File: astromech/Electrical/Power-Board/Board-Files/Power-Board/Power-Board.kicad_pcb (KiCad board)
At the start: 2 copper layers, 119.4 x 96.5 mm, 4 parts

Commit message: loaded components into board
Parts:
- added 12V1: Generic_Power_Out, astromech-footprints:Phoenix-1935161, F.Cu at (263.1, 99.7)
- added 12V2: Generic_Power_Out, astromech-footprints:Phoenix-1935161, F.Cu at (228.2, 116.8)
- added 12V3: Generic_Power_Out, astromech-footprints:Phoenix-1935161, F.Cu at (251.7, 80.9)
- added 12V4: Generic_Power_Out, astromech-footprints:Phoenix-1935161, F.Cu at (239.8, 111.0)
- added 3.3V1: Generic_Power_Out, astromech-footprints:Phoenix-1935161, F.Cu at (251.5, 101.6)
- added 3.3V2: Generic_Power_Out, astromech-footprints:Phoenix-1935161, F.Cu at (251.5, 111.0)
- added 3.3V3: Generic_Power_Out, astromech-footprints:Phoenix-1935161, F.Cu at (280.5, 92.1)
- added 3.3V4: Generic_Power_Out, astromech-footprints:Phoenix-1935161, F.Cu at (297.6, 63.8)
- added 5V1: Generic_Power_Out, astromech-footprints:Phoenix-1935161, F.Cu at (280.5, 82.6)
- added 5V2: Generic_Power_Out, astromech-footprints:Phoenix-1935161, F.Cu at (286.0, 63.8)
- added 5V3: Generic_Power_Out, astromech-footprints:Phoenix-1935161, F.Cu at (263.1, 109.2)
- added 5V4: Generic_Power_Out, astromech-footprints:Phoenix-1935161, F.Cu at (289.8, 54.4)
- added C1: 0.1uF, Capacitor_SMD:C_1206_3216Metric_Pad1.33x1.80mm_HandSolder, F.Cu at (237.3, 117.6)
- added C2: 1u, Capacitor_SMD:C_1206_3216Metric_Pad1.33x1.80mm_HandSolder, F.Cu at (272.2, 102.2)
- added C3: C_T, Capacitor_SMD:C_1206_3216Metric_Pad1.33x1.80mm_HandSolder, F.Cu at (249.4, 117.6)
- added C4: 0.1uF, Capacitor_SMD:C_1206_3216Metric_Pad1.33x1.80mm_HandSolder, F.Cu at (243.3, 117.6)
- added C5: 0.1uF, Capacitor_SMD:C_1206_3216Metric_Pad1.33x1.80mm_HandSolder, F.Cu at (205.1, 118.1)
- added C6: 1u, Capacitor_SMD:C_1206_3216Metric_Pad1.33x1.80mm_HandSolder, F.Cu at (255.4, 117.6)
- added C7: C_T, Capacitor_SMD:C_1206_3216Metric_Pad1.33x1.80mm_HandSolder, F.Cu at (211.1, 118.1)
- added C8: 0.1uF, Capacitor_SMD:C_1206_3216Metric_Pad1.33x1.80mm_HandSolder, F.Cu at (217.1, 118.1)
- added F1: F_MAIN, Fuse:Fuseholder_Blade_Mini_Keystone_3568, F.Cu at (258.9, 52.3)
- added HV_OUT1: HV_OUT, astromech-footprints:Phoenix-1935161, F.Cu at (313.0, 54.4)
- added HV_OUT2: HV_OUT, astromech-footprints:Phoenix-1935161, F.Cu at (234.1, 92.2)
- added HV_OUT3: HV_OUT, astromech-footprints:Phoenix-1935161, F.Cu at (257.3, 90.3)
- added HV_OUT4: HV_OUT, astromech-footprints:Phoenix-1935161, F.Cu at (228.2, 107.4)
- added J1: BAT_IN_SCREW, astromech-footprints:Molex-393900102, F.Cu at (81.3, 91.4)
- added J10: HEAD_MOT, astromech-footprints:Phoenix-1935161, F.Cu at (274.9, 73.2)
- added J2: BAT_IN_HOLE, astromech-footprints:10AWG-Power-In, F.Cu at (96.5, 91.4)
- added J5: E_STOP, astromech-footprints:Phoenix-1935161, F.Cu at (268.9, 88.5)
- added J6: CTRL_BRD, astromech-footprints:Phoenix-1935161, F.Cu at (301.4, 54.4)
- added J7: JETSON, astromech-footprints:Phoenix-1935161, F.Cu at (286.6, 73.2)
- added J8: L_DRIVE, astromech-footprints:Phoenix-1935161, F.Cu at (274.4, 63.8)
- added J9: R_DRIVE, astromech-footprints:Phoenix-1935161, F.Cu at (239.8, 101.6)
- added LV_IN1: LV_IN, astromech-footprints:Phoenix-1935161, F.Cu at (263.3, 79.0)
- added LV_IN2: LV_IN, astromech-footprints:Phoenix-1935161, F.Cu at (278.2, 54.4)
- added LV_IN3: LV_IN, astromech-footprints:Phoenix-1935161, F.Cu at (245.7, 92.2)
- added LV_IN4: LV_IN, astromech-footprints:Phoenix-1935161, F.Cu at (298.2, 73.2)
- added Q1: Q_NMOS_DSG, astromech-footprints:NTMTS0D6N04CLTXG, F.Cu at (308.9, 64.5)
- added Q2: Q_NMOS_DSG, astromech-footprints:NTMTS0D6N04CLTXG, F.Cu at (291.2, 83.4)
- added R1: 220k, Resistor_SMD:R_1206_3216Metric_Pad1.30x1.75mm_HandSolder, F.Cu at (327.7, 51.5)
- added R10: 100k, Resistor_SMD:R_1206_3216Metric_Pad1.30x1.75mm_HandSolder, F.Cu at (316.4, 64.2)
- added R11: R_FLT, Resistor_SMD:R_1206_3216Metric_Pad1.30x1.75mm_HandSolder, F.Cu at (316.4, 60.9)
- added R12: R_G, Resistor_SMD:R_1206_3216Metric_Pad1.30x1.75mm_HandSolder, F.Cu at (278.1, 101.9)
- added R2: 100k, Resistor_SMD:R_1206_3216Metric_Pad1.30x1.75mm_HandSolder, F.Cu at (322.4, 58.7)
- added R3: 100k, Resistor_SMD:R_1206_3216Metric_Pad1.30x1.75mm_HandSolder, F.Cu at (289.6, 90.2)
- added R4: 100k, Resistor_SMD:R_1206_3216Metric_Pad1.30x1.75mm_HandSolder, F.Cu at (307.2, 71.3)
- added R5: R_FLT, Resistor_SMD:R_1206_3216Metric_Pad1.30x1.75mm_HandSolder, F.Cu at (261.3, 119.0)
- added R6: R_G, Resistor_SMD:R_1206_3216Metric_Pad1.30x1.75mm_HandSolder, F.Cu at (298.8, 79.7)
- added R7: 220k, Resistor_SMD:R_1206_3216Metric_Pad1.30x1.75mm_HandSolder, F.Cu at (277.8, 98.6)
- added R8: 100k, Resistor_SMD:R_1206_3216Metric_Pad1.30x1.75mm_HandSolder, F.Cu at (272.1, 105.5)
- added R9: 100k, Resistor_SMD:R_1206_3216Metric_Pad1.30x1.75mm_HandSolder, F.Cu at (261.3, 115.7)
- added TP1: TestPoint, TestPoint:TestPoint_Pad_D2.0mm, F.Cu at (271.4, 80.1)
- added TP2: TestPoint, TestPoint:TestPoint_Pad_D2.0mm, F.Cu at (230.6, 99.1)
- added U1: LTC7003, astromech-footprints:LTC7003, F.Cu at (272.0, 96.9)
- added U2: Logic_Level_Converter, astromech-footprints:Sparkfun-Level-shifter, F.Cu at (262.0, 66.5)
- added U3: D36V50Fx, astromech-footprints:D36V50Fx, F.Cu at (215.3, 63.1)
- added U4: LTC7003, astromech-footprints:LTC7003, F.Cu at (321.9, 53.4)
- added U5: D36V50Fx, astromech-footprints:D36V50Fx, F.Cu at (215.3, 89.6)
- added U6: D36V50Fx, astromech-footprints:D36V50Fx, F.Cu at (241.8, 63.1)

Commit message: grouped related components and did minor layout
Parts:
- U3: value D36V50Fx -> 12V_REG
- U5: value D36V50Fx -> 5V_REG
- U6: value D36V50Fx -> 3.3V_REG
- moved U5 194.0 mm to (405.1, 129.5)
- moved R2 191.1 mm to (138.4, 110.5)
- moved R1 189.8 mm to (147.3, 110.5)
- moved HV_OUT4 172.9 mm to (391.2, 49.5)
- moved R4 169.2 mm to (138.4, 83.0)
- moved F1 160.8 mm to (99.9, 76.1), turned to 90 degrees
- moved R3 151.2 mm to (138.4, 94.5), turned to 180 degrees
- moved 5V3 149.7 mm to (412.8, 111.8)
- moved 5V4 147.3 mm to (425.4, 111.8)
- moved Q1 143.2 mm to (170.2, 100.3)
- moved R6 138.4 mm to (162.6, 104.1)
- moved C2 133.8 mm to (138.4, 99.5), turned to 180 degrees
- moved 5V2 123.7 mm to (400.1, 111.8)
- moved U1 120.9 mm to (151.1, 95.2), turned to -90 degrees
- moved TP1 117.2 mm to (156.2, 101.6)
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
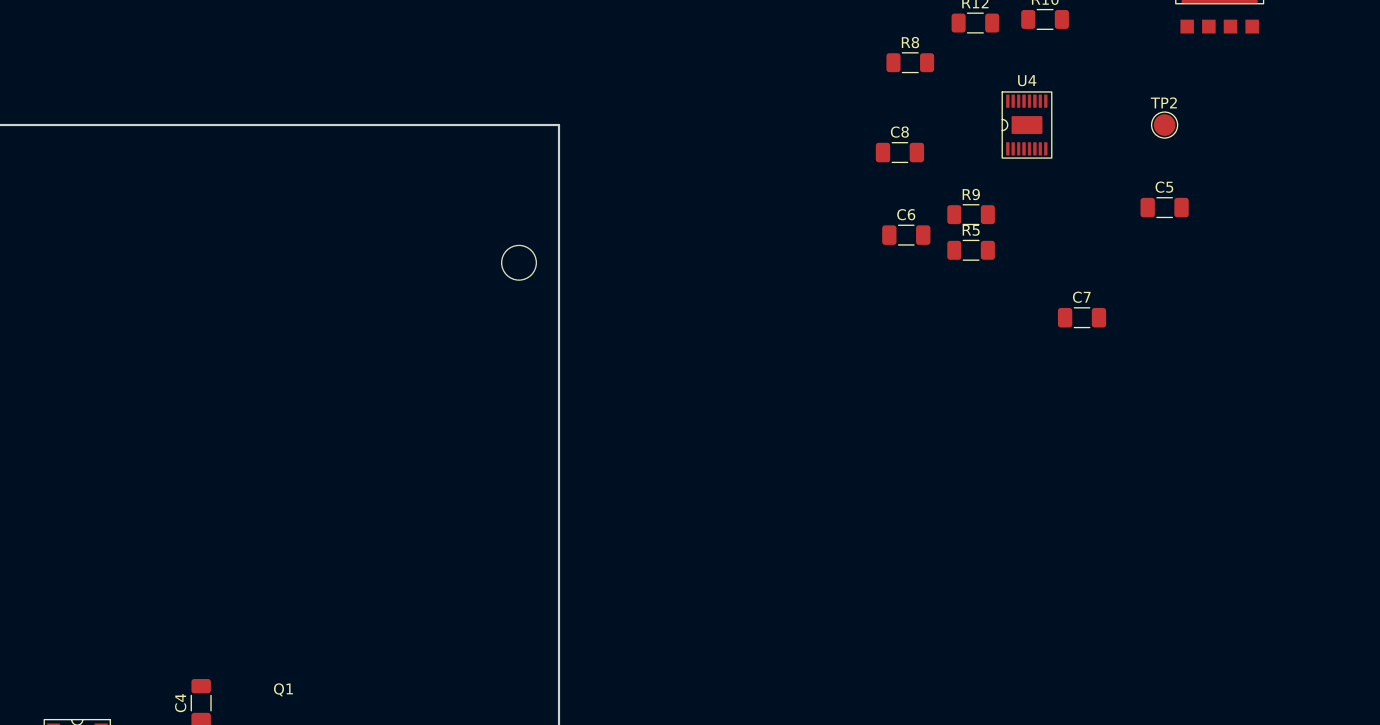
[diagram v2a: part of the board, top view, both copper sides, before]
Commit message: Assigned shottky diode footprints
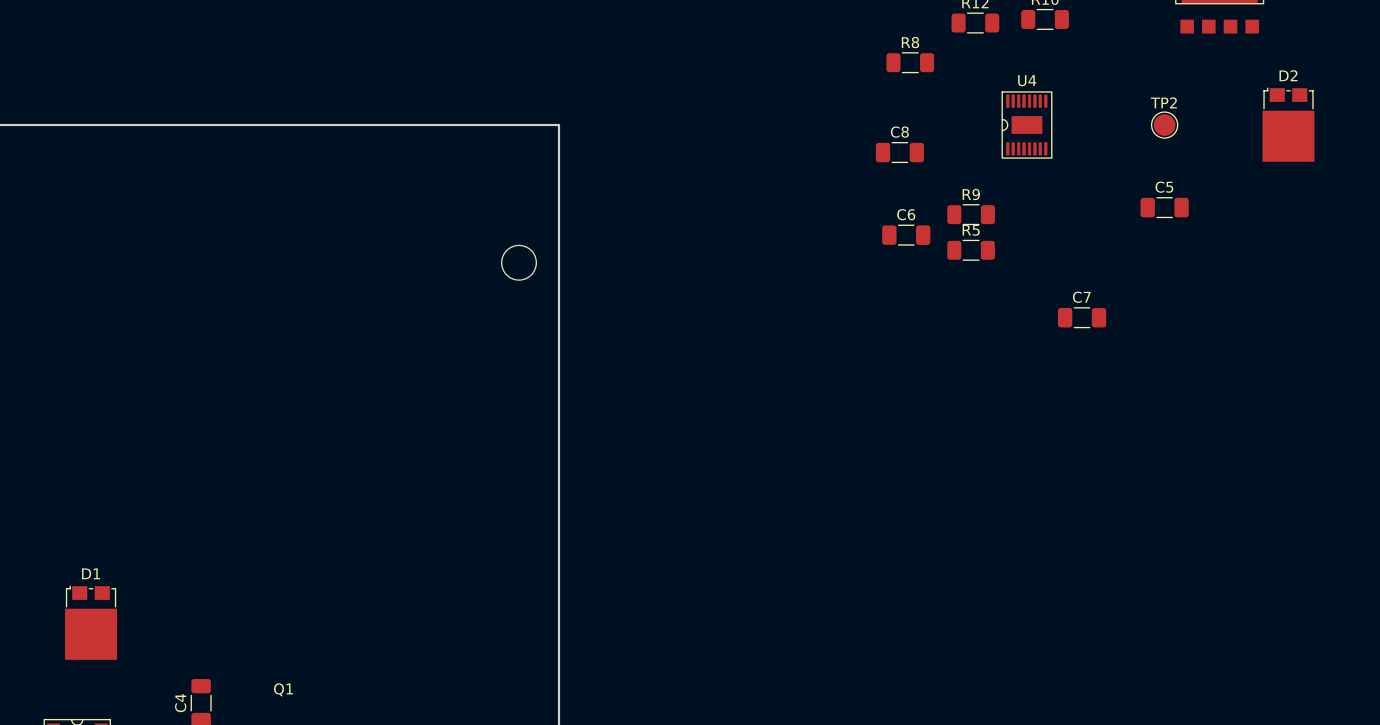
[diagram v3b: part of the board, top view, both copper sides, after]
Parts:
- added D1: D_Schottky_AAK, Package_TO_SOT_SMD:TO-277A, F.Cu at (152.4, 84.0)
- added D2: D_Schottky_AAK, Package_TO_SOT_SMD:TO-277A, F.Cu at (262.9, 38.1)
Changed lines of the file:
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@@
   (net 54 "unconnected-(U6-Pad5)")
   (net 55 "unconnected-(U6-Pad6)")
+  (net 56 "unconnected-(D2-Pad1)")
   (footprint "Resistor_SMD:R_1206_3216Metric_Pad1.30x1.75mm_HandSolder" (layer "F.Cu")
     (at 233.6025 49.66)
@@
     (pad "2" thru_hole roundrect (at 2.54 0) (size 2 4.5) (drill 1.3) (layers *.Cu *.Mask) (roundrect_rratio 0.5)
       (net 3 "5V_REG") (pinfunction "+") (pintype "power_in"))
+  )
+  (footprint "Package_TO_SOT_SMD:TO-277A" (layer "F.Cu")
+    (at 152.4 84.05)
+    (descr "Thermal enhanced ultra thin SMD package; 3 leads; body: 4.3x6.1x0.43mm, https://www.vishay.com/docs/95570/to-277asmpc.pdf")
+    (tags "TO-277A SMPC")
+    (property "Sheetfile" "Power-Board.kicad_sch")
+    (property "Sheetname" "")
+    (attr smd)
+    (fp_text reference "D1" (at 0 -4.5 -180) (layer "F.SilkS")
+      (effects (font (size 1 1) (thickness 0.15)))
+    )
+    (fp_text value "D_Schottky_AAK" (at 0 4.5 -180) (layer "F.Fab")
+      (effects (font (size 1 1) (thickness 0.15)))
+    )
+    (fp_text user "${REFERENCE}" (at 0 0) (layer "F.Fab")
+      (effects (font (size 1 1) (thickness 0.15)))
+    )
+    (fp_line (start 2.26 -1.5) (end 2.26 -3.16) (layer "F.SilkS") (width 0.12))
+    (fp_line (start -1.92 -3.4) (end -1.92 -3.16) (layer "F.SilkS") (width 0.12))
+    (fp_line (start 2.26 -3.16) (end 1.92 -3.16) (layer "F.SilkS") (width 0.12))
+    (fp_line (start -0.16 -3.16) (end 0.16 -3.16) (layer "F.SilkS") (width 0.12))
+    (fp_line (start -2.26 -3.16) (end -2.26 -1.5) (layer "F.SilkS") (width 0.12))
+    (fp_line (start -1.92 -3.16) (end -2.26 -3.16) (layer "F.SilkS") (width 0.12))
+    (fp_line (start 2.65 3.65) (end -2.65 3.65) (layer "F.CrtYd") (width 0.05))
+    (fp_line (start -2.65 -3.65) (end 2.65 -3.65) (layer "F.CrtYd") (width 0.05))
+    (fp_line (start -2.65 -3.65) (end -2.65 3.65) (layer "F.CrtYd") (width 0.05))
+    (fp_line (start 2.65 3.65) (end 2.65 -3.65) (layer "F.CrtYd") (width 0.05))
+    (fp_line (start 2.15 3.05) (end 2.15 -3.05) (layer "F.Fab") (width 0.1))
+    (fp_line (start 2.15 -3.05) (end -1.15 -3.05) (layer "F.Fab") (width 0.1))
+    (fp_line (start -2.15 3.05) (end 2.15 3.05) (layer "F.Fab") (width 0.1))
+    (fp_line (start -1.15 -3.05) (end -2.15 -2.05) (layer "F.Fab") (width 0.1))
+    (fp_line (start -2.15 -2.05) (end -2.15 3.05) (layer "F.Fab") (width 0.1))
+    (pad "" smd rect (at -1.7 -0.65 180) (size 1.25 1.2) (layers "F.Paste"))
+    (pad "" smd rect (at 1.7 2.7) (size 1.25 1.2) (layers "F.Paste"))
+    (pad "" smd rect (at 1.7 1.04) (size 1.25 1.2) (layers "F.Paste"))
+    (pad "" smd rect (at 0 1.04) (size 1.25 1.2) (layers "F.Paste"))
+    (pad "" smd rect (at -1.7 2.7) (size 1.25 1.2) (layers "F.Paste"))
+    (pad "" smd rect (at -1.7 1.04) (size 1.25 1.2) (layers "F.Paste"))
+    (pad "" smd rect (at 0 -0.65) (size 1.25 1.2) (layers "F.Paste"))
+    (pad "" smd rect (at 0 2.7) (size 1.25 1.2) (layers "F.Paste"))
+    (pad "" smd rect (at 1.7 -0.65) (size 1.25 1.2) (layers "F.Paste"))
+    (pad "1" smd rect (at -1.04 -2.765) (size 1.4 1.27) (layers "F.Cu" "F.Paste" "F.Mask")
+      (net 1 "GND") (pinfunction "A") (pintype "passive"))
+    (pad "2" smd rect (at 1.04 -2.765) (size 1.4 1.27) (layers "F.Cu" "F.Paste" "F.Mask")
+      (net 1 "GND") (pinfunction "A") (pintype "passive"))
+    (pad "3" smd rect (at 0 1.04) (size 4.8 4.72) (layers "F.Cu" "F.Mask")
+      (net 9 "+BATT") (pinfunction "K") (pintype "passive"))
+    (model "${KICAD6_3DMODEL_DIR}/Package_TO_SOT_SMD.3dshapes/TO-277A.wrl"
+      (offset (xyz 0 0 0))
+      (scale (xyz 1 1 1))
+      (rotate (xyz 0 0 0))
+    )
   )
   (footprint "astromech-footprints:Phoenix-1935161" (layer "F.Cu")
@@
       (offset (xyz 0 0 0))
       (scale (xyz 1 1 1))
+      (rotate (xyz 0 0 0))
+    )
+  )
+  (footprint "Package_TO_SOT_SMD:TO-277A" (layer "F.Cu")
+    (at 262.89 38.1)
+    (descr "Thermal enhanced ultra thin SMD package; 3 leads; body: 4.3x6.1x0.43mm, https://www.vishay.com/docs/95570/to-277asmpc.pdf")
+    (tags "TO-277A SMPC")
+    (property "Sheetfile" "Power-Board.kicad_sch")
+    (property "Sheetname" "")
+    (attr smd)
+    (fp_text reference "D2" (at 0 -4.5 -180) (layer "F.SilkS")
+      (effects (font (size 1 1) (thickness 0.15)))
+    )
+    (fp_text value "D_Schottky_AAK" (at 0 4.5 -180) (layer "F.Fab")
+      (effects (font (size 1 1) (thickness 0.15)))
+    )
+    (fp_text user "${REFERENCE}" (at 0 0) (layer "F.Fab")
+      (effects (font (size 1 1) (thickness 0.15)))
+    )
+    (fp_line (start -1.92 -3.4) (end -1.92 -3.16) (layer "F.SilkS") (width 0.12))
+    (fp_line (start 2.26 -1.5) (end 2.26 -3.16) (layer "F.SilkS") (width 0.12))
+    (fp_line (start 2.26 -3.16) (end 1.92 -3.16) (layer "F.SilkS") (width 0.12))
+    (fp_line (start -2.26 -3.16) (end -2.26 -1.5) (layer "F.SilkS") (width 0.12))
+    (fp_line (start -1.92 -3.16) (end -2.26 -3.16) (layer "F.SilkS") (width 0.12))
+    (fp_line (start -0.16 -3.16) (end 0.16 -3.16) (layer "F.SilkS") (width 0.12))
+    (fp_line (start 2.65 3.65) (end -2.65 3.65) (layer "F.CrtYd") (width 0.05))
+    (fp_line (start -2.65 -3.65) (end -2.65 3.65) (layer "F.CrtYd") (width 0.05))
+    (fp_line (start -2.65 -3.65) (end 2.65 -3.65) (layer "F.CrtYd") (width 0.05))
+    (fp_line (start 2.65 3.65) (end 2.65 -3.65) (layer "F.CrtYd") (width 0.05))
+    (fp_line (start -1.15 -3.05) (end -2.15 -2.05) (layer "F.Fab") (width 0.1))
+    (fp_line (start -2.15 -2.05) (end -2.15 3.05) (layer "F.Fab") (width 0.1))
+    (fp_line (start -2.15 3.05) (end 2.15 3.05) (layer "F.Fab") (width 0.1))
+    (fp_line (start 2.15 -3.05) (end -1.15 -3.05) (layer "F.Fab") (width 0.1))
+    (fp_line (start 2.15 3.05) (end 2.15 -3.05) (layer "F.Fab") (width 0.1))
+    (pad "" smd rect (at 1.7 1.04) (size 1.25 1.2) (layers "F.Paste"))
+    (pad "" smd rect (at -1.7 2.7) (size 1.25 1.2) (layers "F.Paste"))
+    (pad "" smd rect (at -1.7 -0.65 180) (size 1.25 1.2) (layers "F.Paste"))
+    (pad "" smd rect (at -1.7 1.04) (size 1.25 1.2) (layers "F.Paste"))
+    (pad "" smd rect (at 1.7 -0.65) (size 1.25 1.2) (layers "F.Paste"))
+    (pad "" smd rect (at 0 2.7) (size 1.25 1.2) (layers "F.Paste"))
+    (pad "" smd rect (at 0 -0.65) (size 1.25 1.2) (layers "F.Paste"))
+    (pad "" smd rect (at 1.7 2.7) (size 1.25 1.2) (layers "F.Paste"))
+    (pad "" smd rect (at 0 1.04) (size 1.25 1.2) (layers "F.Paste"))
+    (pad "1" smd rect (at -1.04 -2.765) (size 1.4 1.27) (layers "F.Cu" "F.Paste" "F.Mask")
+      (net 56 "unconnected-(D2-Pad1)") (pinfunction "A") (pintype "passive"))
+    (pad "2" smd rect (at 1.04 -2.765) (size 1.4 1.27) (layers "F.Cu" "F.Paste" "F.Mask")
+      (net 1 "GND") (pinfunction "A") (pintype "passive"))
+    (pad "3" smd rect (at 0 1.04) (size 4.8 4.72) (layers "F.Cu" "F.Mask")
+      (net 13 "MOT_VOLTAGE") (pinfunction "K") (pintype "passive"))
+    (model "${KICAD6_3DMODEL_DIR}/Package_TO_SOT_SMD.3dshapes/TO-277A.wrl"
+      (offset (xyz 0 0 0))
+      (scale (xyz 1 1 1))

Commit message: Modified level converter connections
Made to fit NEO encoder connection order
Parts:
- added C10: C_G, Capacitor_SMD:C_1206_3216Metric_Pad1.33x1.80mm_HandSolder, F.Cu at (151.1, 124.8)
- added C9: C_G, Capacitor_SMD:C_1206_3216Metric_Pad1.33x1.80mm_HandSolder, F.Cu at (381.0, 234.3)
- added R13: R_CGDAMP, Resistor_SMD:R_1206_3216Metric_Pad1.30x1.75mm_HandSolder, F.Cu at (151.1, 140.3)
- added R14: R_CGDAMP, Resistor_SMD:R_1206_3216Metric_Pad1.30x1.75mm_HandSolder, F.Cu at (151.1, 117.9)
- moved R5 169.4 mm to (75.6, 110.7)
- moved R7 137.4 mm to (123.2, 107.1), turned to 90 degrees
- moved R8 132.1 mm to (123.2, 112.8), turned to 90 degrees
- moved Q2 131.7 mm to (137.2, 80.6), turned to 90 degrees
- moved TP2 127.9 mm to (156.8, 124.2)
- moved C5 127.1 mm to (138.4, 103.9), turned to -90 degrees
- moved D2 122.8 mm to (162.6, 109.0), turned to 180 degrees
- moved J5 121.1 mm to (125.7, 55.2), turned to 180 degrees
- moved R10 120.9 mm to (143.5, 100.7), turned to -90 degrees
- moved C7 118.3 mm to (138.4, 109.6), turned to -90 degrees
- moved J10 118.2 mm to (114.4, 55.2), turned to 180 degrees
- moved R12 117.9 mm to (156.8, 117.9), turned to -90 degrees
- moved R9 117.2 mm to (133.3, 107.1), turned to -90 degrees
- moved J9 117.0 mm to (103.0, 55.2), turned to 180 degrees
- moved J8 115.8 mm to (91.5, 55.2), turned to 180 degrees
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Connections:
- D2 pad 1: unconnected-(D2-Pad1) -> GND
- R12 pad 1: Net-(R12-Pad1) -> Net-(U4-Pad12)
- R6 pad 1: Net-(R6-Pad1) -> Net-(U1-Pad12)
- TP1 pad 1: Net-(R6-Pad1) -> Net-(Q1-Pad3)
- TP2 pad 1: Net-(R12-Pad1) -> Net-(Q2-Pad3)
- U1 pad 11: Net-(R6-Pad1) -> Net-(Q1-Pad3)
- U1 pad 12: Net-(R6-Pad1) -> Net-(U1-Pad12)
- U4 pad 11: Net-(R12-Pad1) -> Net-(Q2-Pad3)
- U4 pad 12: Net-(R12-Pad1) -> Net-(U4-Pad12)
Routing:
- added copper zone on F.Cu, net +BATT
- added copper zone on F.Cu, net Net-(F1-Pad1)
- added copper zone on F.Cu, net POW+

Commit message: Assigned screw terminal to switch
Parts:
- removed HV_OUT1, HV_OUT2, HV_OUT3, HV_OUT4: HV_OUT, astromech-footprints:Phoenix-1935161
- removed LV_IN1, LV_IN2, LV_IN3, LV_IN4: LV_IN, astromech-footprints:Phoenix-1935161
- added S1: illuminated_switch, astromech-footprints:Phoenix-1935187, F.Cu at (52.1, 85.1)
- added SIG-CONV-HV1: Screw_Term_04, astromech-footprints:Phoenix-1935187, F.Cu at (303.5, 35.5)
- added SIG-CONV-HV2: Screw_Term_04, astromech-footprints:Phoenix-1935187, F.Cu at (325.1, 19.7)
- added SIG-CONV-LV1: Screw_Term_03, astromech-footprints:Phoenix-1935174, F.Cu at (382.7, 35.5)
- added SIG-CONV-LV2: Screw_Term_03, astromech-footprints:Phoenix-1935174, F.Cu at (388.0, 24.1)
- moved U5 276.0 mm to (139.7, 54.0)
- moved U6 242.0 mm to (100.3, 20.3)
- moved U3 219.5 mm to (73.7, 20.3)
- moved J10 139.3 mm to (252.8, 70.5)
- moved J5 139.3 mm to (264.2, 70.5)
- moved J8 139.3 mm to (229.9, 70.5)
- moved J9 139.3 mm to (241.4, 70.5)
- moved J6 112.6 mm to (156.5, 31.1), turned to 180 degrees
- moved J7 95.3 mm to (168.3, 31.1), turned to 180 degrees
- moved C4 49.5 mm to (77.5, 156.6)
- moved R1 49.5 mm to (59.1, 167.4)
- moved R2 49.5 mm to (53.3, 167.4)
- moved R4 49.5 mm to (53.3, 149.0)
- moved R6 49.5 mm to (77.5, 167.4)
- moved TP1 49.5 mm to (71.1, 166.8)
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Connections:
- U2 pad 1: Net-(HV_OUT4-Pad2) -> /ENCB_HV1
- U2 pad 2: Net-(HV_OUT3-Pad2) -> /ENCA_HV1
- U2 pad 4: Net-(HV_OUT2-Pad2) -> /ENCB_HV2
- U2 pad 5: Net-(HV_OUT1-Pad2) -> /ENCA_HV1
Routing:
- added copper zone on B.Cu, net GND
